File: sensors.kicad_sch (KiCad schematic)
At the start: 9 parts, among them IC4 BME690, U2 BME280, U3 BMP581

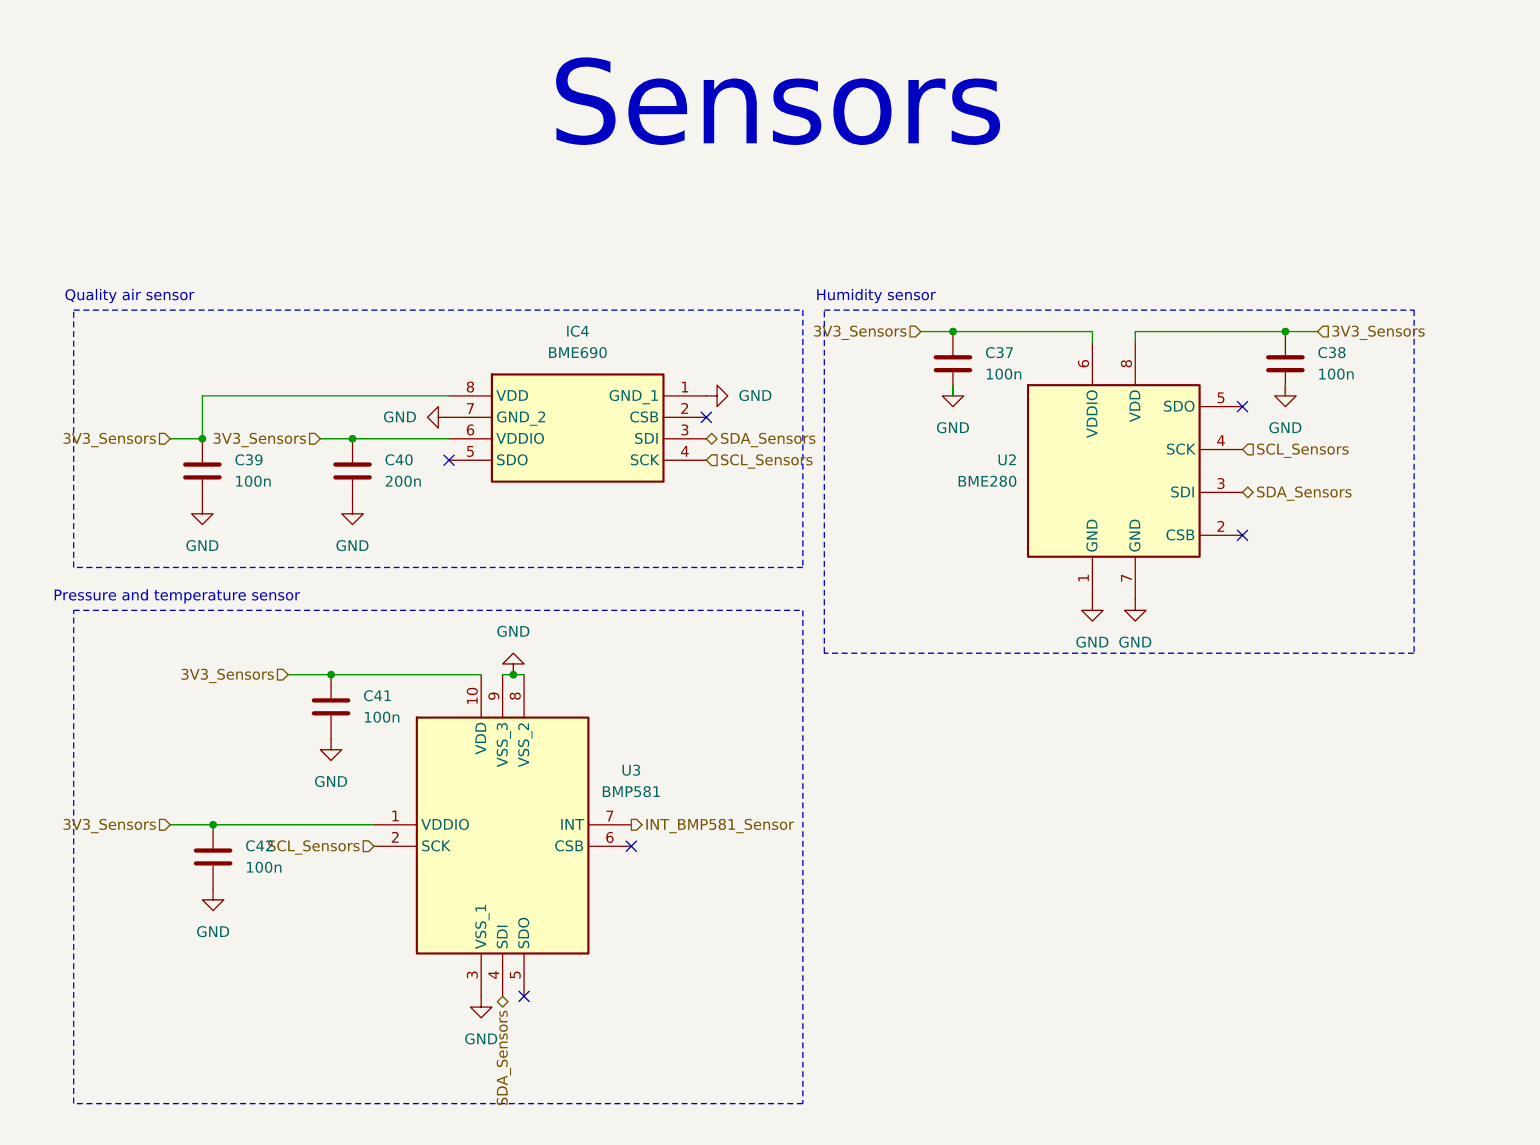
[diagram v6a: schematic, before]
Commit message: Update schematic to Kicad 10
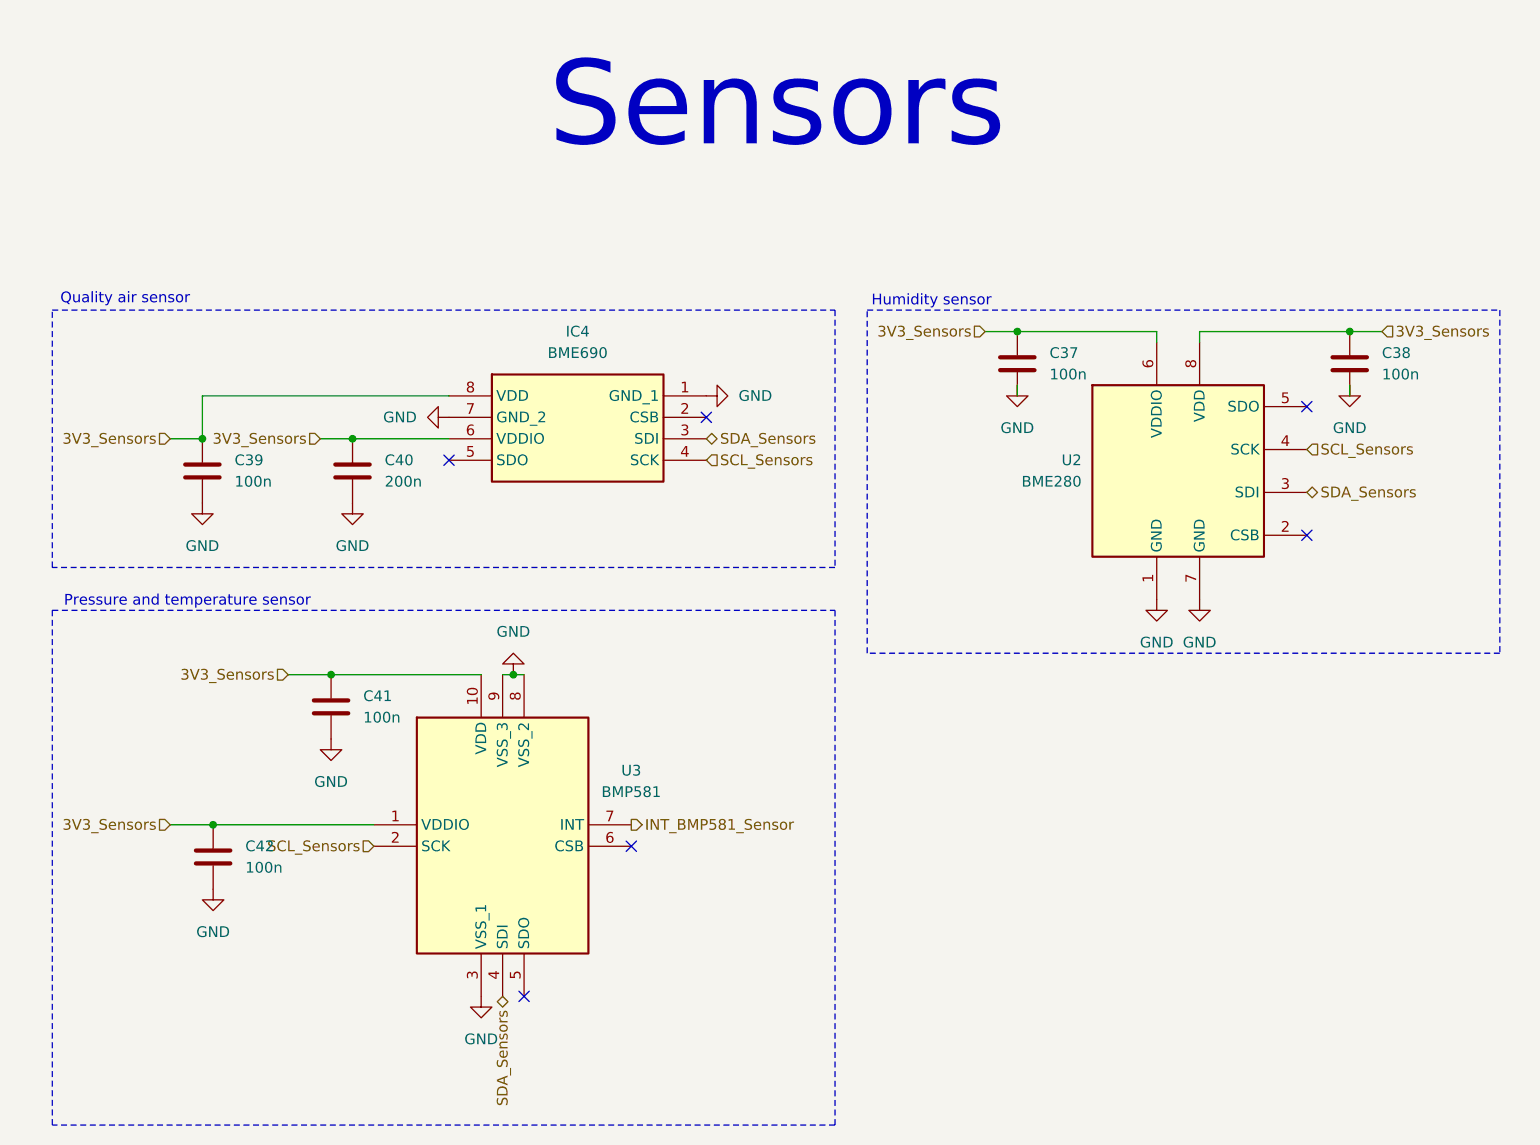
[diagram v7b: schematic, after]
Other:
- moved on the sheet: C37, C38, U2

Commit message: Add tests points with 5015 footprint for practicity
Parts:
- renumbered C39 to C37, C42 to C38, C41 to C39, C37 to C41, C38 to C42, U3 to U2, U2 to U3
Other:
- moved on the sheet: C41, C42, U3
